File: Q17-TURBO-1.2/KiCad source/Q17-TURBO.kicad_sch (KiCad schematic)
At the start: 93 parts, among them J1 INPUT, J2 SPK+, J3 DC, Q1 IRF610, Q10 KSA992, Q12 KSC1845, Q13 IRF610, Q14 IRF9610, Q15 FQA46N15, Q16 IXTH48P20P, Q17 FQA46N15, Q18 IXTH48P20P, Q2 KSA992, Q3 KSC1845, Q4 IRF9610, Q5 FQPF7P20, Q6 2SK3564, Q7 LSK170B, Q8 DN2540, Q9 BS250P, U1 OPA1611, U2 NDC7003P

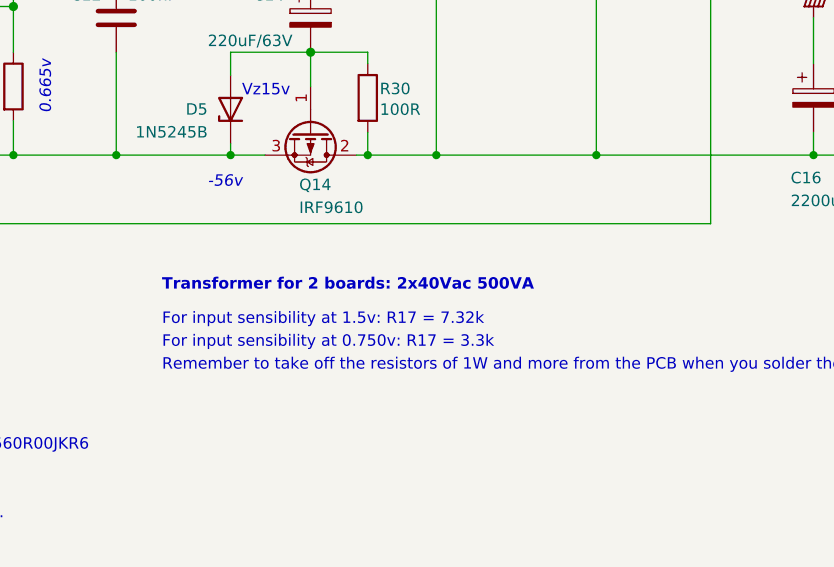
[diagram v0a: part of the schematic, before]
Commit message: Update Q17-Turbo to 1.2.2
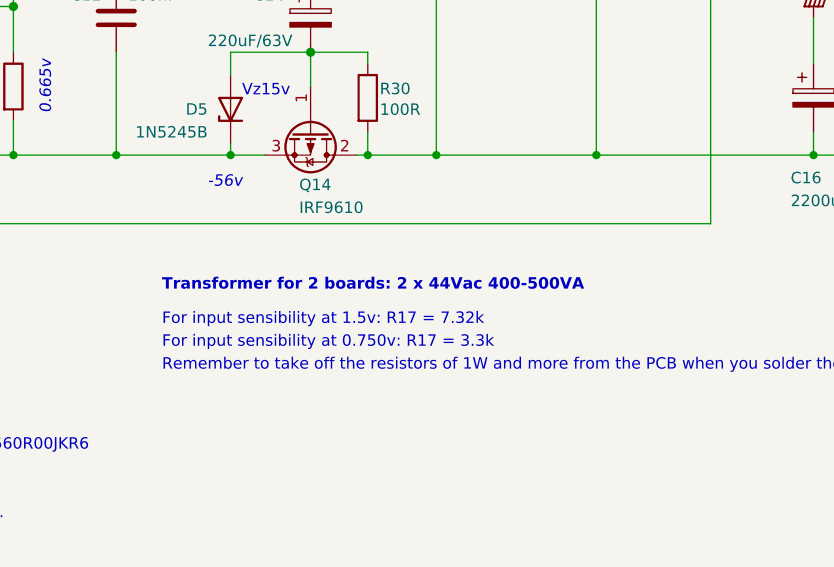
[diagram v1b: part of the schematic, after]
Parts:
- R24: Mouser 594-MRS25000C1009FRP -> 594-MRS2510K00F; Part# MRS25000C1009FRP00 -> MRS25000C1002FRP00
- U1: footprint Q17_Library:SOIC-8_3.9x4.9mm_P1.27mm_handsoldering -> Package_SO:SOIC-8_3.9x4.9mm_P1.27mm
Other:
- note added: "Transformer for 2 boards: 2 x 44Vac 400-500VA"
- note removed: "Transformer for 2 boards: 2x40Vac 500VA"
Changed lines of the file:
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@@
   (title_block
     (title "Q17-TURBO (P2) Amplifier")
-    (date "2023-08-06")
-    (rev "1.2.1")
+    (date "2023-09-04")
+    (rev "1.2.4")
     (company "by eng. Tiberiu Vicol")
     (comment 1 "Modified by Stef for the Q17-TURBO project")
@@
     (effects (font (size 1.27 1.27)) (justify left bottom))
   )
-  (text "Transformer for 2 boards: 2x40Vac 500VA" (at 177.8 156.21 0)
+  (text "Transformer for 2 boards: 2 x 44Vac 400-500VA" (at 177.8 156.21 0)
     (effects (font (size 1.27 1.27) (thickness 0.254) bold) (justify left bottom))
   )
@@
       (effects (font (size 1.27 1.27)) (justify left))
     )
-    (property "Footprint" "Q17_Library:SOIC-8_3.9x4.9mm_P1.27mm_handsoldering" (at 66.04 76.2 0)
+    (property "Footprint" "Package_SO:SOIC-8_3.9x4.9mm_P1.27mm" (at 66.04 76.2 0)
       (effects (font (size 1.27 1.27)) hide)
     )
@@
       (effects (font (size 1.27 1.27)) hide)
     )
-    (property "Part#" "MRS25000C1009FRP00" (at 128.27 64.77 0)
+    (property "Part#" "MRS25000C1002FRP00" (at 128.27 64.77 0)
       (effects (font (size 1.27 1.27)) hide)
     )
-    (property "Mouser" "594-MRS25000C1009FRP" (at 128.27 64.77 0)
+    (property "Mouser" "594-MRS2510K00F" (at 128.27 64.77 0)
       (effects (font (size 1.27 1.27)) hide)
     )

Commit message: Update schematic for Q17-Turbo 1.2
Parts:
- R11, R12: Mouser 71-CCF0247R0JKE36 -> 594-5083NW47R00J; Part# CCF0247R0JKE36 -> PR02000204709JR500
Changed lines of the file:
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@@
   (title_block
     (title "Q17-TURBO (P2) Amplifier")
-    (date "2023-09-04")
+    (date "2023-09-05")
     (rev "1.2.4")
     (company "by eng. Tiberiu Vicol")
@@
       (effects (font (size 1.27 1.27)) hide)
     )
-    (property "Datasheet" "https://www.vishay.com/doc?31012" (at 161.29 68.58 0)
-      (effects (font (size 1.27 1.27)) hide)
-    )
-    (property "Part#" "CCF0247R0JKE36" (at 161.29 68.58 0)
-      (effects (font (size 1.27 1.27)) hide)
-    )
-    (property "Mouser" "71-CCF0247R0JKE36" (at 161.29 68.58 0)
+    (property "Datasheet" "https://www.vishay.com/doc?28729" (at 161.29 68.58 0)
+      (effects (font (size 1.27 1.27)) hide)
+    )
+    (property "Part#" "PR02000204709JR500" (at 161.29 68.58 0)
+      (effects (font (size 1.27 1.27)) hide)
+    )
+    (property "Mouser" "594-5083NW47R00J" (at 161.29 68.58 0)
       (effects (font (size 1.27 1.27)) hide)
     )
@@
       (effects (font (size 1.27 1.27)) hide)
     )
-    (property "Datasheet" "https://www.vishay.com/doc?31012" (at 161.29 99.06 0)
-      (effects (font (size 1.27 1.27)) hide)
-    )
-    (property "Part#" "CCF0247R0JKE36" (at 161.29 99.06 0)
-      (effects (font (size 1.27 1.27)) hide)
-    )
-    (property "Mouser" "71-CCF0247R0JKE36" (at 161.29 99.06 0)
-      (effects (font (size 1.27 1.27)) hide)
-    )
+    (property "Datasheet" "https://www.vishay.com/doc?28729" (at 161.29 99.06 0)
+      (effects (font (size 1.27 1.27)) hide)
+    )
+    (property "Part#" "PR02000204709JR500" (at 161.29 99.06 0)
+      (effects (font (size 1.27 1.27)) hide)
+    )
+    (property "Mouser" "594-5083NW47R00J" (at 161.29 99.06 0)
+      (effects (font (size 1.27 1.27)) hide)
+    )

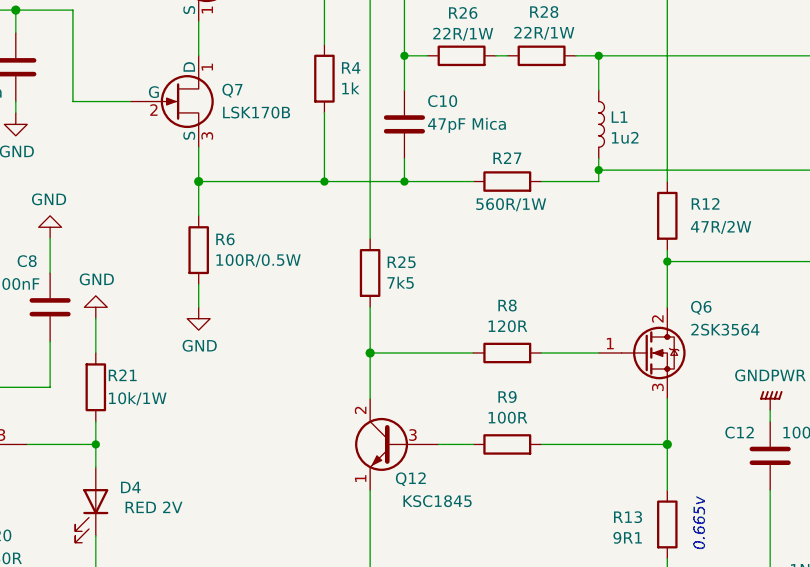
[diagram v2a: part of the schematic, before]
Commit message: Q17-Turbo: Update of R25 value.
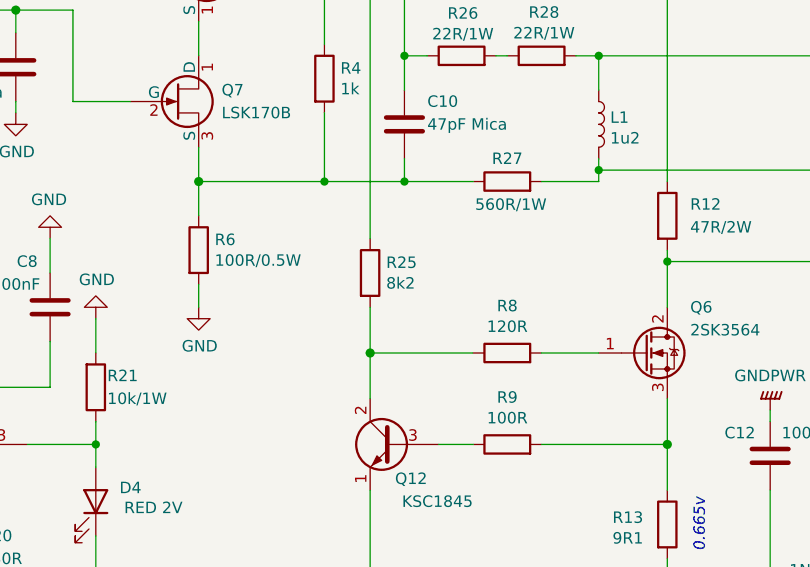
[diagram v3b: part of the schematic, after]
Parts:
- R25: value 7k5 -> 8k2; Mouser 594-MRS25000C7501FRP -> 594-MRS25000C8201FRP; Part# MRS25000C7501FRP00 -> MRS25000C8201FRP00
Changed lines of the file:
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@@
   (title_block
     (title "Q17-TURBO (P2) Amplifier")
-    (date "2023-09-05")
-    (rev "1.2.4")
+    (date "2023-09-14")
+    (rev "1.2.5")
     (company "by eng. Tiberiu Vicol")
     (comment 1 "Modified by Stef for the Q17-TURBO project")
@@
       (effects (font (size 1.27 1.27)) (justify left))
     )
-    (property "Value" "7k5" (at 130.048 106.559 0)
+    (property "Value" "8k2" (at 130.048 106.559 0)
       (effects (font (size 1.27 1.27)) (justify left))
     )
@@
       (effects (font (size 1.27 1.27)) hide)
     )
-    (property "Part#" "MRS25000C7501FRP00" (at 128.27 105.41 0)
+    (property "Part#" "MRS25000C8201FRP00" (at 128.27 105.41 0)
       (effects (font (size 1.27 1.27)) hide)
     )
-    (property "Mouser" "594-MRS25000C7501FRP" (at 128.27 105.41 0)
+    (property "Mouser" "594-MRS25000C8201FRP" (at 128.27 105.41 0)
       (effects (font (size 1.27 1.27)) hide)
     )

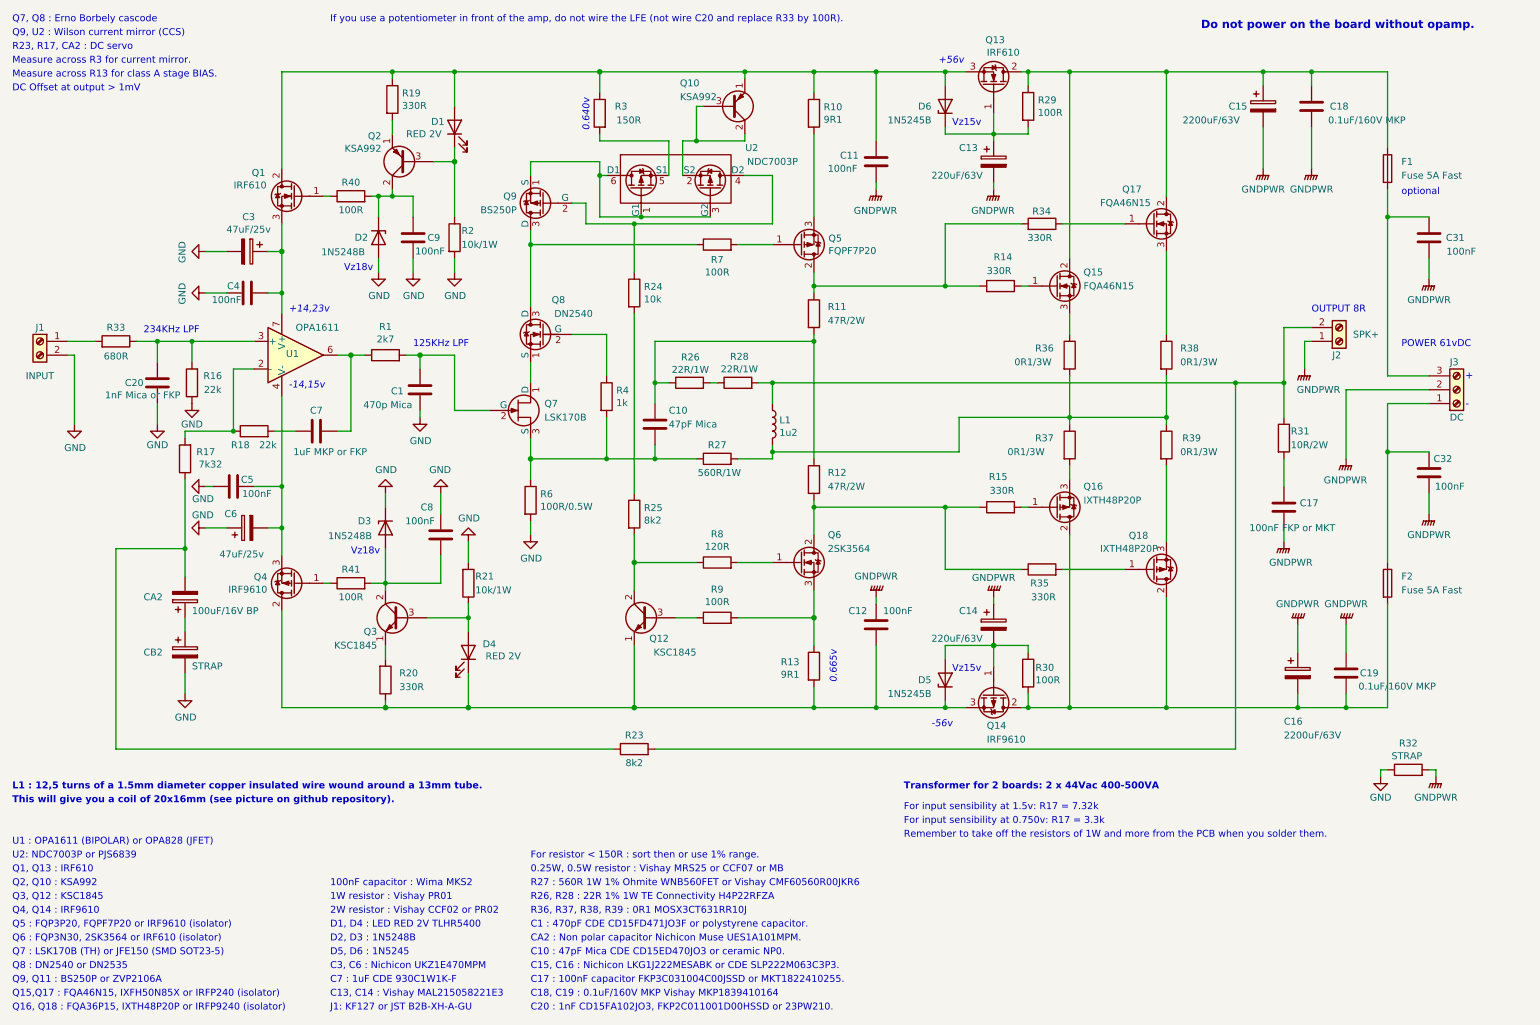
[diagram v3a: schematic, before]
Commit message: Update Q17-Turbo to 1.2.3
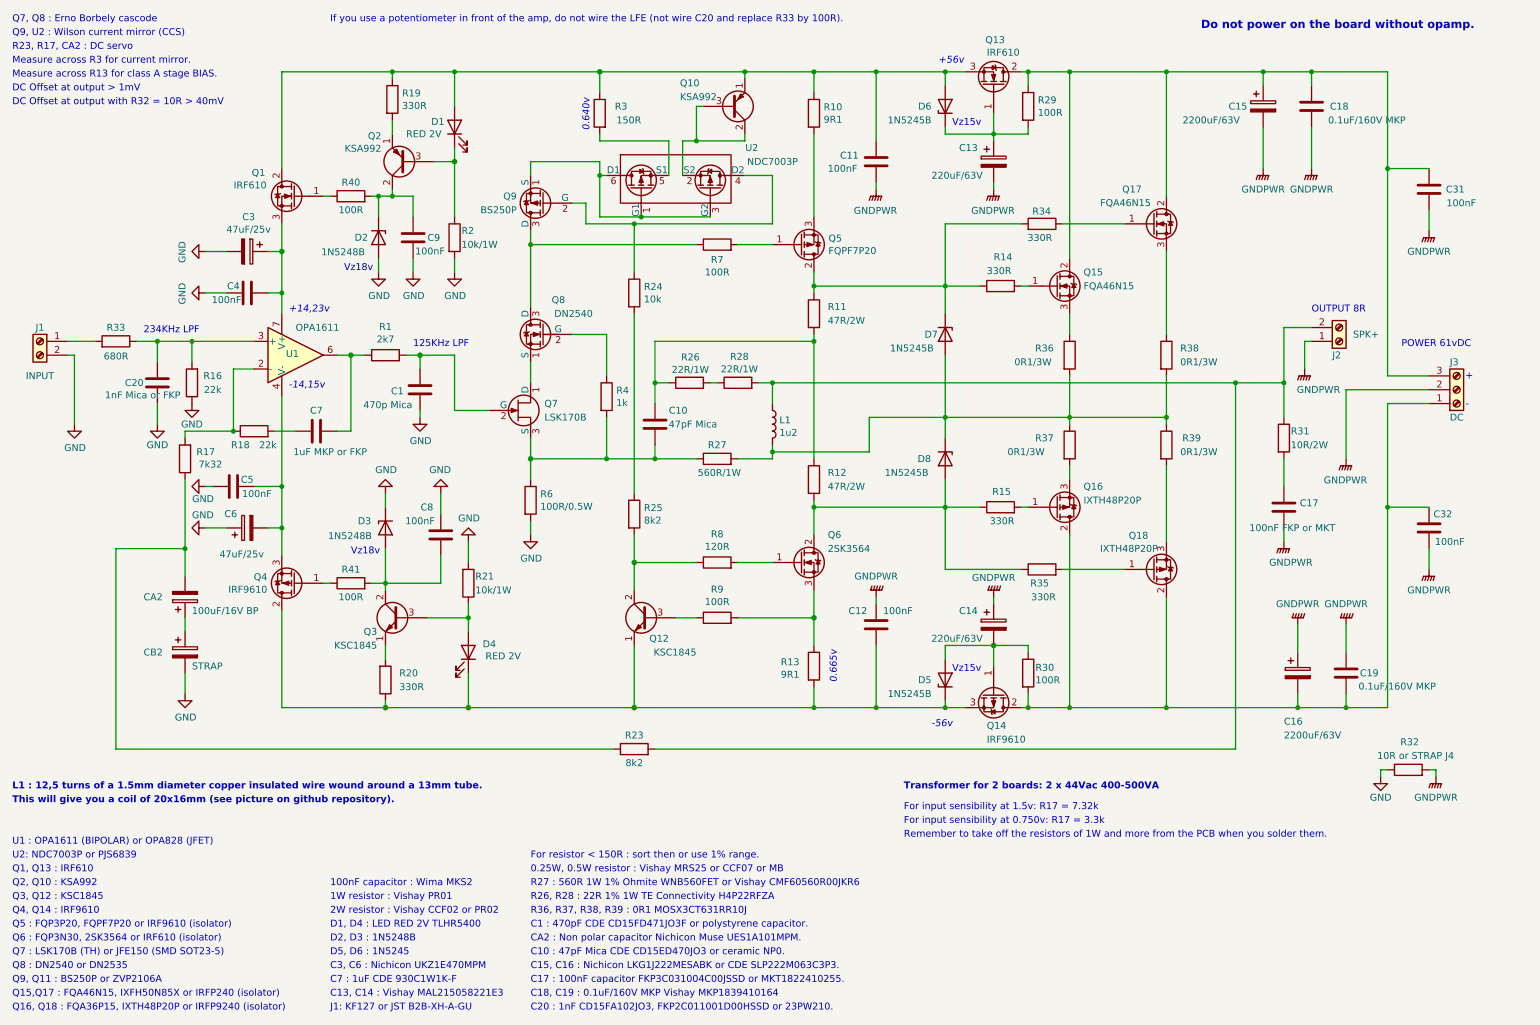
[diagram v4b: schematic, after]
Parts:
- removed F1, F2: Fuse 5A Fast, Q17_Library:fuse_holder_CQ-2-Enlarged, symbol Device:Fuse
- added D7, D8: 1N5245B, Diode_THT:D_DO-35_SOD27_P7.62mm_Horizontal, symbol Device:D_Zener
- J3: footprint TerminalBlock_Phoenix:TerminalBlock_Phoenix_PT-1,5-3-5.0-H_1x03_P5.00mm_Horizontal -> Q17_Library:TerminalBlock_Phoenix_PT-1,5-3-5.0-H_1x03_P5.00mm_Horizontal_Faston
- R32: value STRAP -> 10R or STRAP J4; footprint Resistor_THT:R_Axial_DIN0207_L6.3mm_D2.5mm_P10.16mm_Horizontal -> Q17_Library:THT_POT_Vishay_T93Y_Vertical; Mouser N.A -> 594-MRS25000C1009FRP; Part# STRAP -> MRS25000C1009FRP00
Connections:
- net at L1.2, R27.2, R36.2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: now also D7.2 (A), D8.1 (K)
- net at Q5.2 (D), R11.1, R14.2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: now also D7.1 (K)
- net at C16.2, C19.1, Q14.2 (D)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: now also C32.2, J3.1 (Pin_1)
- net at Q6.2 (D), R12.2, R15.1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: now also D8.2 (A)
- net at C15.1, C18.2, Q13.2 (D)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: now also C31.2, J3.3 (Pin_3)
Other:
- note added: "DC Offset at output with R32 = 10R > 40mV"
- note removed: "optional"
- moved on the sheet: C31, C32
